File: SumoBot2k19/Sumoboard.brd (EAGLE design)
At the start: 37 parts

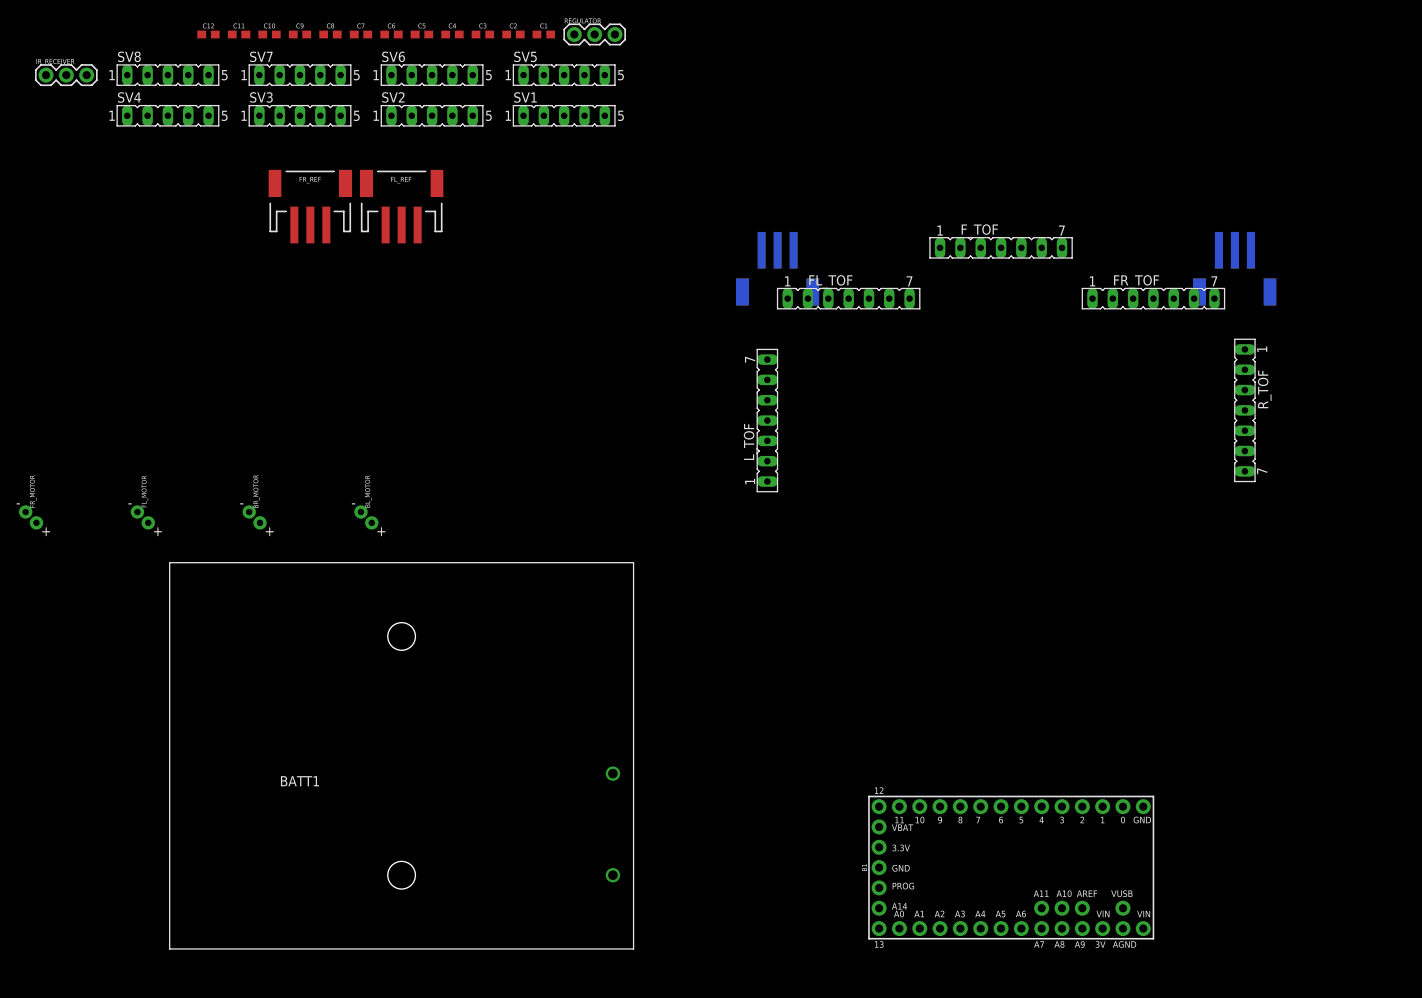
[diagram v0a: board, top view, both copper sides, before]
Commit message: moved the reflectance sensors around, removed the unrouted layer to make things more readable
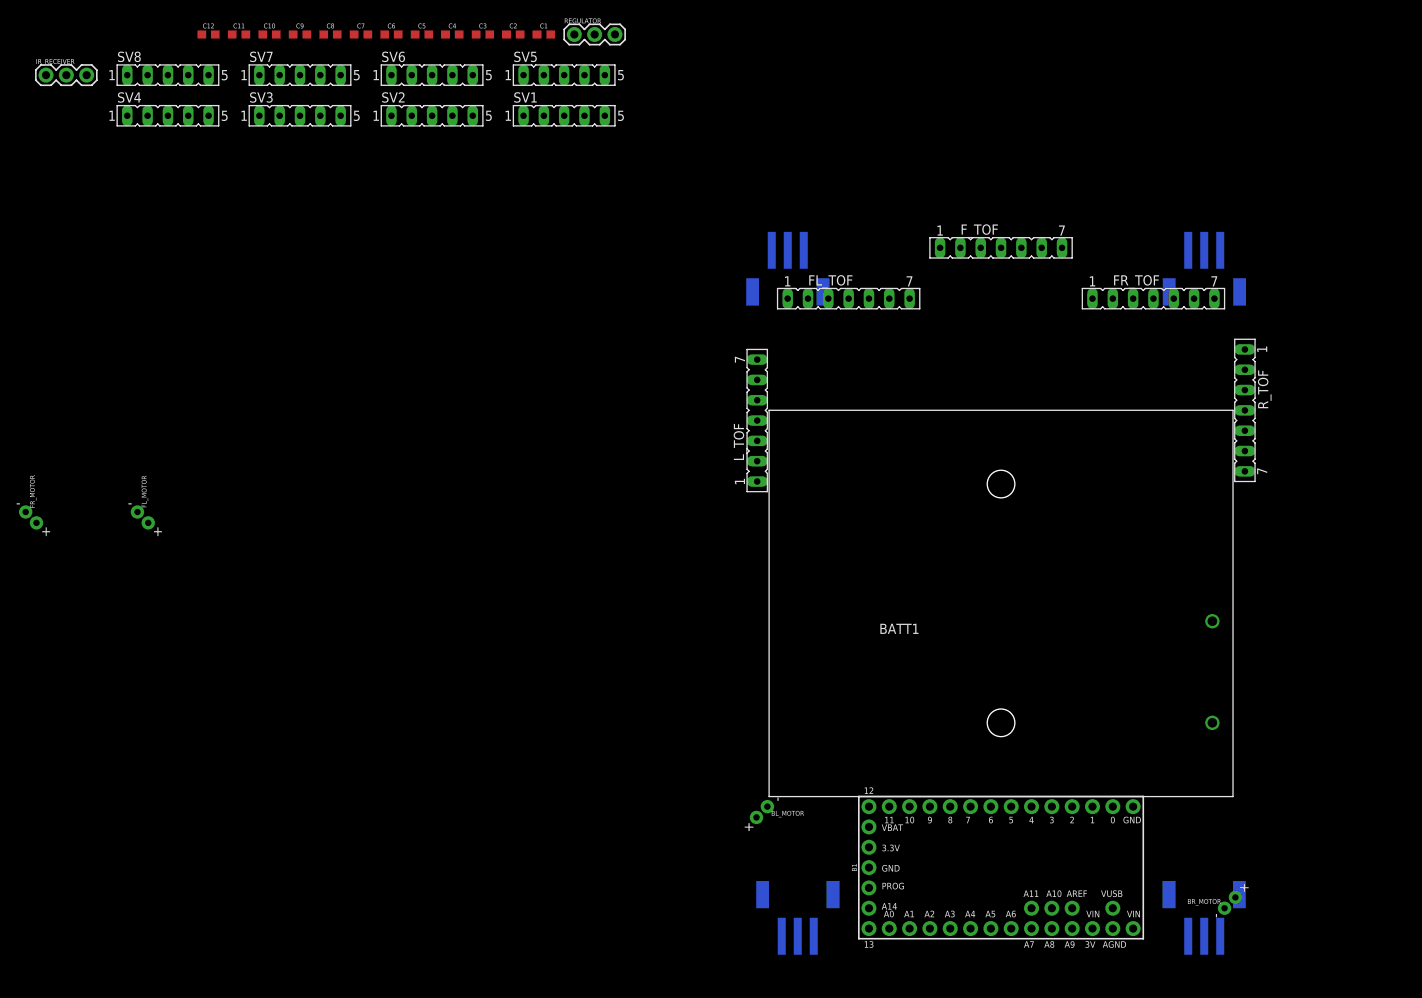
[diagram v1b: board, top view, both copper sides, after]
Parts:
- moved BR_MOTOR 121.9 mm to (58.4, 12.7), turned to 90 degrees
- moved FR_REF 112.5 mm to (58.4, 83.8), flipped to the bottom, turned to 180 degrees
- moved BATT1 77.3 mm to (33.0, 44.5)
- moved BR_REF 76.3 mm to (58.4, 7.62), turned to 0 degrees
- moved BL_REF 76.2 mm to (7.62, 7.62), turned to 0 degrees
- moved BL_MOTOR 65.6 mm to (6.35, 12.7), turned to 270 degrees
- moved FL_REF 49.9 mm to (6.35, 83.8), flipped to the bottom, turned to 180 degrees
- moved L_TOF 1.27 mm to (2.54, 67.3)
- moved B1 1.27 mm to (33.0, 11.4)

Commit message: placed components (all except capacitors) on PCB
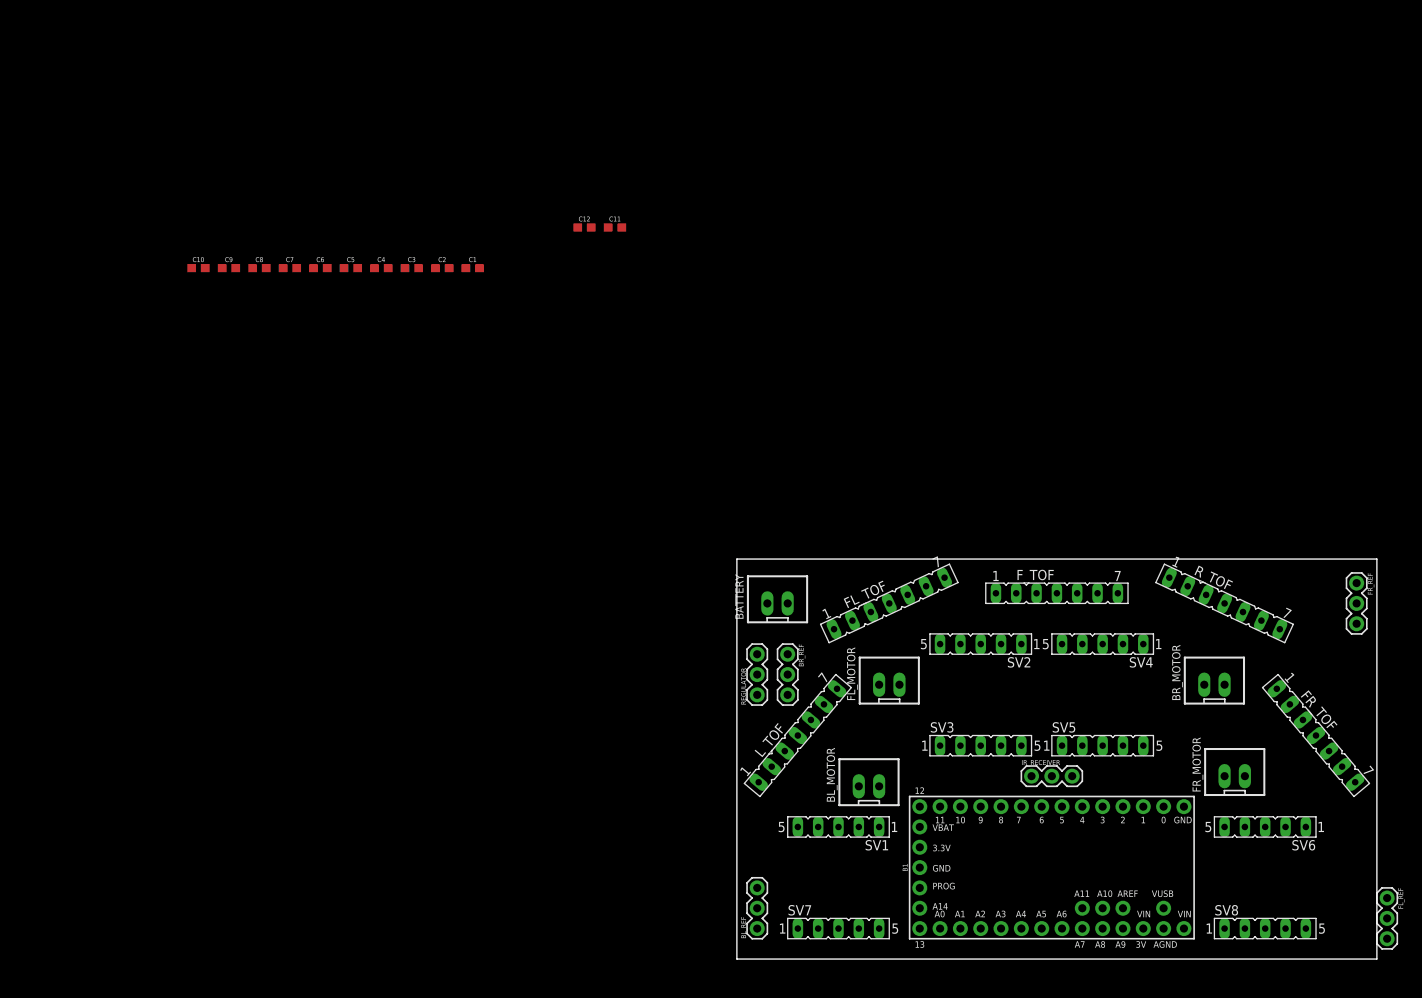
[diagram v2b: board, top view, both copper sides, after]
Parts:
- removed BATT1: 2464_BATT_HOLDER, DC_LOAD_AU:2464BATT_HOLDER
- added BATTERY: JST-XH-02-PIN-LONG-PAD, Rembrandt Electronics - JST XH Connectors v1-0:JST-XH-02-PACKAGE-LONG-PAD
- BL_MOTOR, BR_MOTOR, FL_MOTOR, FR_MOTOR: value MOTOR10MM -> JST-XH-02-PIN-LONG-PAD; device SparkFun-Electromechanical:VIBE-MOTOR-10MM -> Rembrandt Electronics - JST XH Connectors v1-0:JST-XH-02-PACKAGE-LONG-PAD
- BL_REF, BR_REF, FL_REF, FR_REF: value 3-PIN SMD -> (none); device SparkFun-Connectors:JST-3-SMD -> SparkFun-Connectors:1X03
- moved SV8 173.8 mm to (66.0, 3.81)
- moved IR_RECEIVER 151.2 mm to (36.8, 22.9)
- moved FR_MOTOR 149.1 mm to (62.2, 22.9)
- moved SV6 140.3 mm to (66.0, 16.5), turned to 180 degrees
- moved SV4 134.2 mm to (45.7, 39.4), turned to 180 degrees
- moved SV7 126.1 mm to (12.7, 3.81)
- moved SV3 115.9 mm to (30.5, 26.7)
- moved SV5 107.5 mm to (45.7, 26.7)
- moved FL_REF 106.9 mm to (81.3, 7.62), flipped to the top, turned to 270 degrees
- moved SV1 95.3 mm to (12.7, 16.5), turned to 180 degrees
- moved SV2 95.2 mm to (30.5, 39.4), turned to 180 degrees
- moved FL_MOTOR 90.9 mm to (19.1, 34.3)
- moved REGULATOR 85.7 mm to (2.54, 33.0), turned to 90 degrees
- moved BR_REF 60.3 mm to (6.35, 38.1), flipped to the top, turned to 270 degrees
- moved FR_TOF 58.3 mm to (72.4, 27.9), turned to 310 degrees
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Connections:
- removed net BL_PWM: B1.4, SV3.1
- removed net BR_PWM: B1.10, SV8.1
- removed net FL_PWM: B1.3, SV7.1
- removed net FR_PWM: B1.9, SV5.1
- removed net N$15: BL_MOTOR.+, SV2.4
- removed net N$16: BL_MOTOR.-, SV2.3
- removed net N$19: FR_MOTOR.+, SV4.4
- removed net N$20: FR_MOTOR.-, SV4.3
- removed net N$23: BR_MOTOR.+, SV6.4
- removed net N$24: BR_MOTOR.-, SV6.3
- new net LEFT_PWM: B1.3, SV3.1, SV7.1
- new net N$3: BR_MOTOR.1, SV4.4
- new net N$4: BR_MOTOR.2, SV4.3
- new net N$5: FL_MOTOR.1, SV2.4
- new net N$6: FL_MOTOR.2, SV2.3
- new net N$7: FR_MOTOR.1, SV6.4
- new net N$8: FR_MOTOR.2, SV6.3
- new net RIGHT_PWM: B1.9, SV5.1, SV8.1
- net 3.3V: now also C1.1, C2.1, C3.1, C4.1, C5.1, FL_TOF.6, FR_TOF.6, F_TOF.6, L_TOF.6, R_TOF.6
- net GND: now also BATTERY.2; no longer BATT1.-
- net N$1: now also BL_MOTOR.2, SV1.3; no longer FL_MOTOR.+, SV1.4
- net N$2: now also BL_MOTOR.1, SV1.4; no longer FL_MOTOR.-, SV1.3
- net VIN: now also BATTERY.1; no longer BATT1.+, C1.1, C2.1, C3.1, C4.1, C5.1, FL_TOF.6, FR_TOF.6, F_TOF.6, L_TOF.6, R_TOF.6
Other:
- board outline added: 80 x 50 mm

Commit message: moved components
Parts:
- moved FL_REF 3.81 mm to (77.5, 7.62)
- moved BR_REF 1.83 mm to (7.37, 39.6)
- moved REGULATOR 1.80 mm to (3.81, 34.3)
- moved SV8 1.63 mm to (67.1, 2.54)
- moved SV7 1.27 mm to (12.7, 2.54)
- moved BATTERY 1.08 mm to (5.84, 45.2)
- moved B1 0.64 mm to (40.0, 11.4)

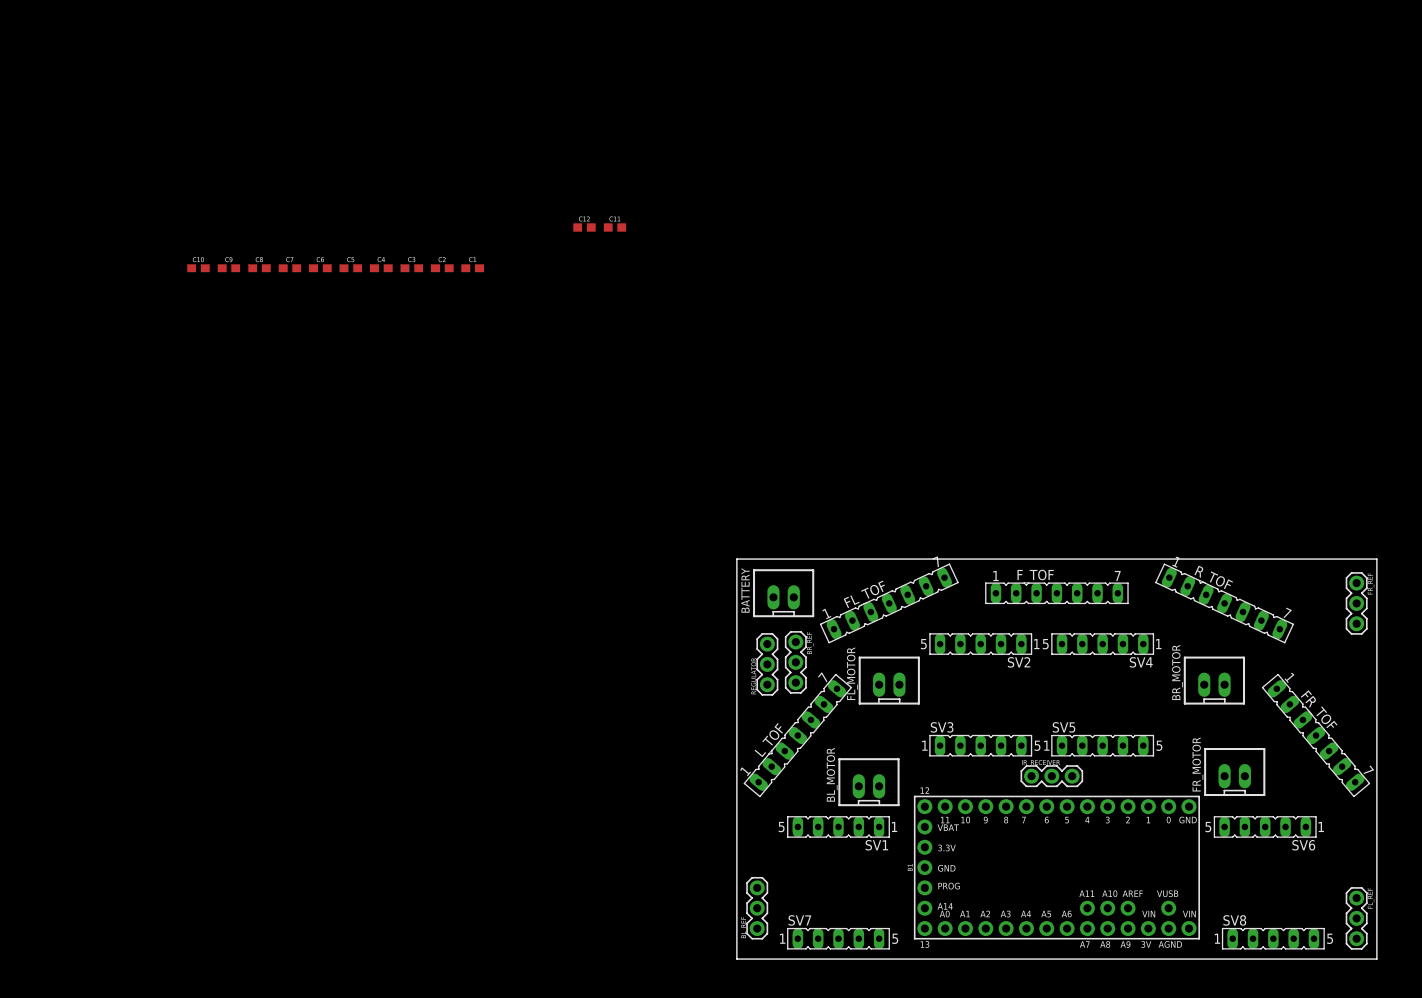
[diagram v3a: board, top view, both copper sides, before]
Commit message: placed capacitors
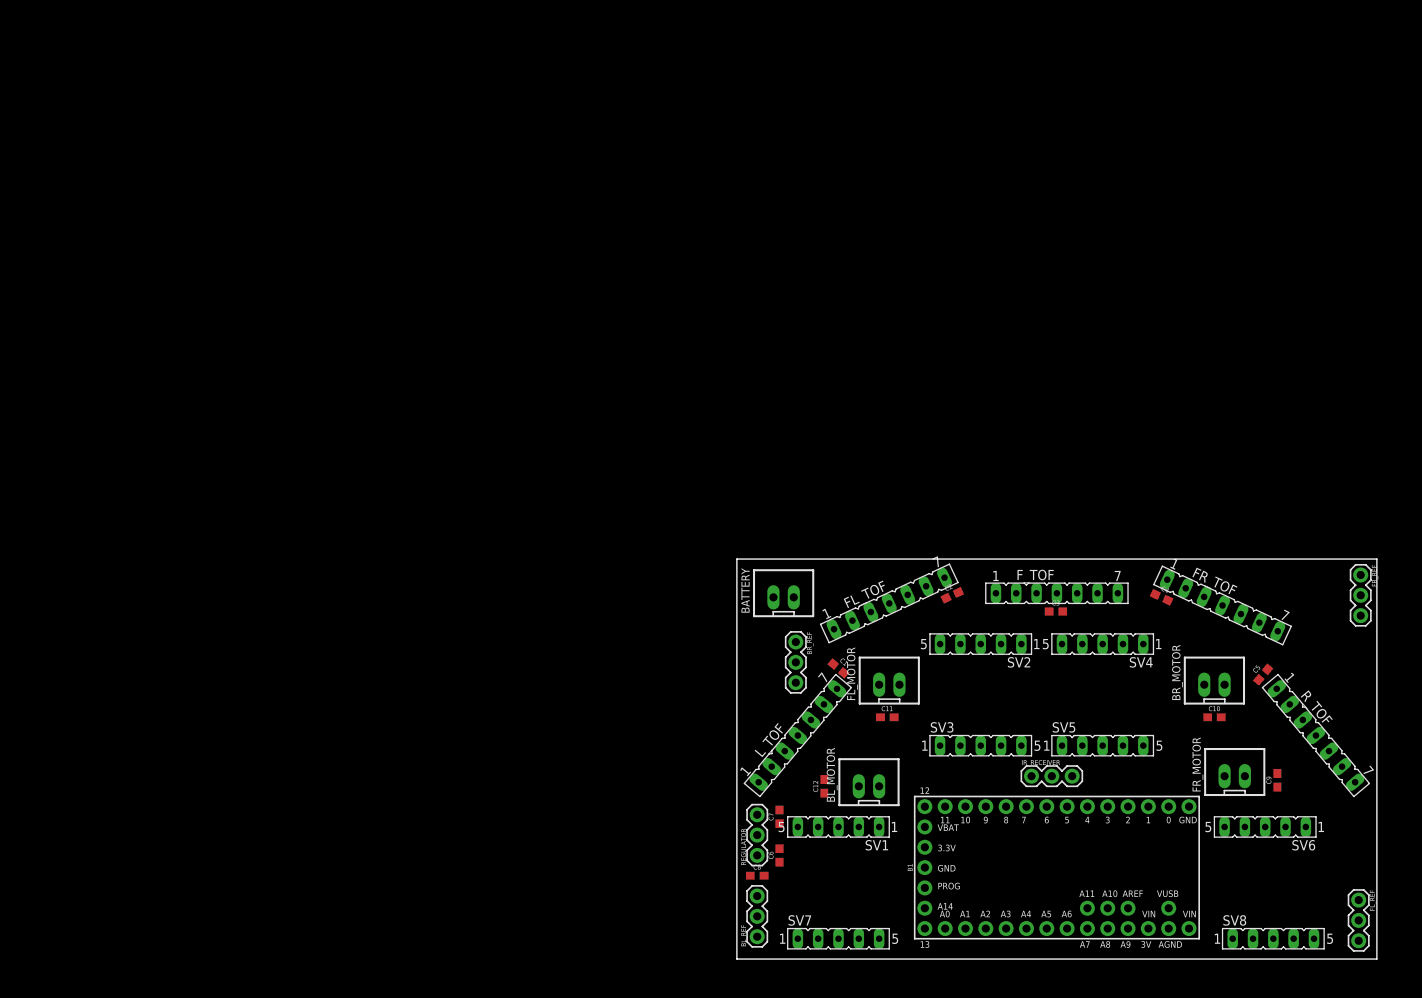
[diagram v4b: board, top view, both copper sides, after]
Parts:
- moved C9 145.9 mm to (67.6, 22.4), turned to 90 degrees
- moved C10 138.9 mm to (59.7, 30.2)
- moved C5 124.8 mm to (65.8, 35.6), turned to 50 degrees
- moved C4 105.9 mm to (53.1, 45.2), turned to 335 degrees
- moved C8 98.2 mm to (2.54, 10.4)
- moved C6 93.2 mm to (5.33, 13.0), turned to 90 degrees
- moved C7 91.9 mm to (5.33, 17.8), turned to 90 degrees
- moved C3 91.2 mm to (39.9, 43.4)
- moved C12 76.0 mm to (10.9, 21.6), turned to 90 degrees
- moved C2 75.7 mm to (26.9, 45.5), turned to 25 degrees
- moved C11 70.0 mm to (18.8, 30.2)
- moved C1 67.8 mm to (12.7, 36.3), turned to 320 degrees
- moved REGULATOR 21.4 mm to (2.54, 13.0)
- moved R_TOF 20.1 mm to (72.4, 27.9), turned to 310 degrees
- moved FR_TOF 20.0 mm to (60.7, 44.2), turned to 335 degrees
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
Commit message: added connection needs checking
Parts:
- moved BR_REF 4.85 mm to (2.54, 40.1)
- moved C3 3.31 mm to (43.2, 43.2)
- moved C4 1.70 mm to (52.3, 43.7)
- moved C7 0.51 mm to (5.33, 18.3)
- moved C5 0.25 mm to (66.0, 35.6)
- moved C6 0.25 mm to (5.33, 12.7)
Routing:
- net SDA: track 0.00 -> 53.8 mm

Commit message: tweeks here and there
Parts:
- moved SV1 1.27 mm to (14.0, 16.5)
- moved SV7 1.27 mm to (14.0, 2.54)
- moved BL_MOTOR 1.27 mm to (16.5, 22.9)
- moved SV8 1.02 mm to (66.0, 2.54)
- moved IR_RECEIVER 0.76 mm to (37.6, 22.9)
- moved FR_REF 0.51 mm to (77.5, 48.0)
- moved FL_REF 0.25 mm to (77.5, 7.37)
